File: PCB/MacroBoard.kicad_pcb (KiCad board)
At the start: 2 copper layers, 192.1 x 82.6 mm, 57 parts, among them J1 Pwr, J2 UART, J3 ADC, J4 I2C, J5 B In, J6 Switch, SW0 SW_Push, SW1 SW_Push, SW10 SW_Push, SW11 SW_Push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

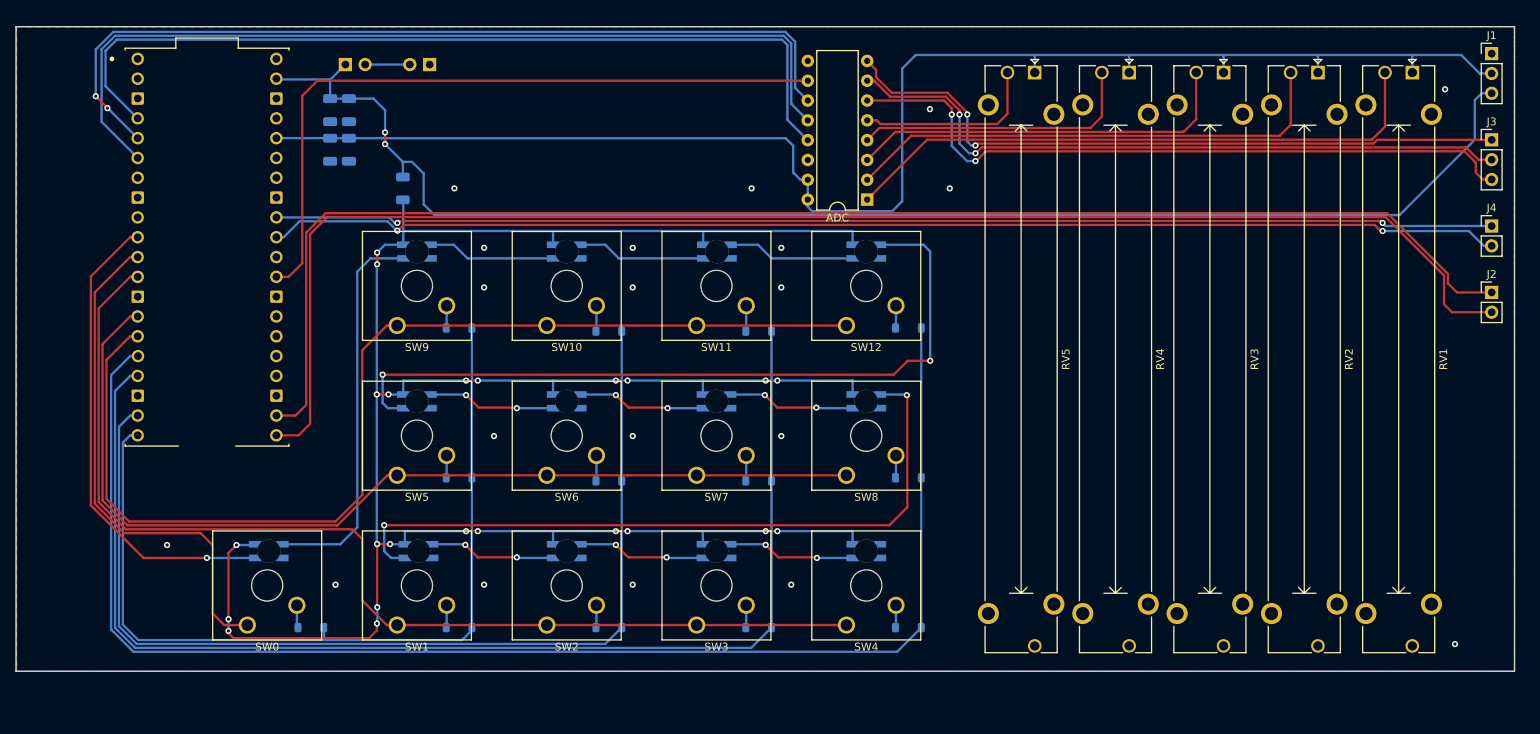
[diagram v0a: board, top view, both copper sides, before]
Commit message: Increased power tracks width
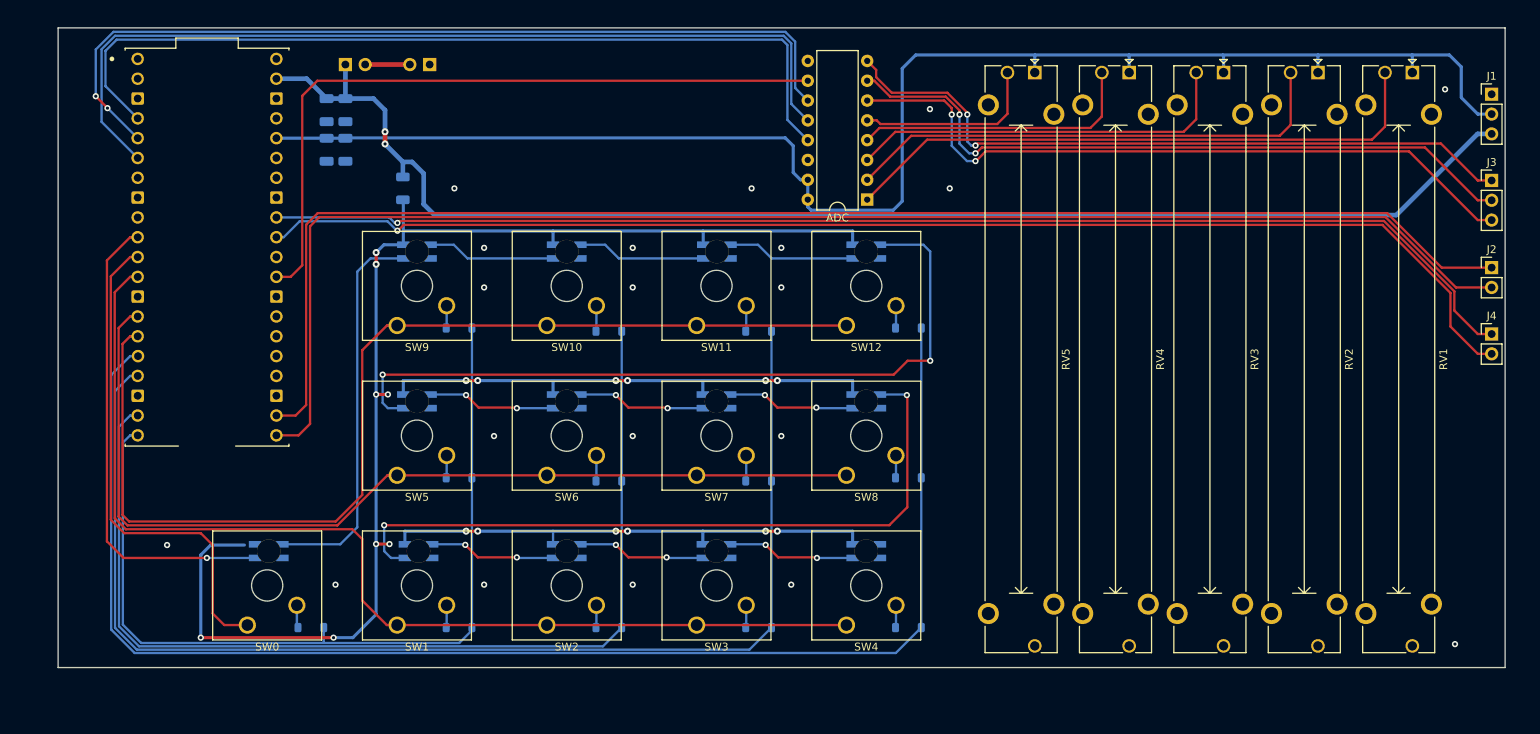
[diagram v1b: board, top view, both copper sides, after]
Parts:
- moved J4 13.8 mm to (209.2, 56.8)
- moved J3 5.21 mm to (209.2, 37.1)
- moved J1 5.21 mm to (209.2, 26.0)
- moved J2 3.18 mm to (209.2, 48.3)
- moved C1 0.45 mm to (62.2, 33.1)
- moved C2 0.45 mm to (59.8, 33.1)
- moved C3 0.45 mm to (59.8, 28.1)
- moved C4 0.45 mm to (62.2, 28.1)
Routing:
- net I2C_SDA_E: track 158.6 -> 166.8 mm, vias 2 -> 1
- net I2C_SCL_E: track 156.5 -> 163.6 mm, vias 2 -> 1
- net 5V: track 183.5 -> 178.6 mm
- net 3V3: track 194.6 -> 197.9 mm
- net UART_TX: track 188.8 -> 186.0 mm
- net CH_6: track 87.4 -> 89.5 mm
- net CH_7: track 87.6 -> 89.3 mm
- net ROW_2: track 125.4 -> 123.7 mm
- net ROW_1: track 140.4 -> 138.7 mm
- net ROW_3: track 138.5 -> 136.8 mm
- net ROW_4: track 65.8 -> 64.1 mm
- net UART_RX: track 184.4 -> 183.0 mm
- net CH_5: track 88.8 -> 90.3 mm
- net LED: track 290.8 -> 291.8 mm, vias 23 -> 20
- net COL_1: track 112.4 -> 113.1 mm
- removed copper zone on B.Cu, net GND
- removed copper zone on F.Cu, net GND
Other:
- board size 192.1 x 82.6 mm -> 185.5 x 82 mm

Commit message: New LED Footprint, new routings
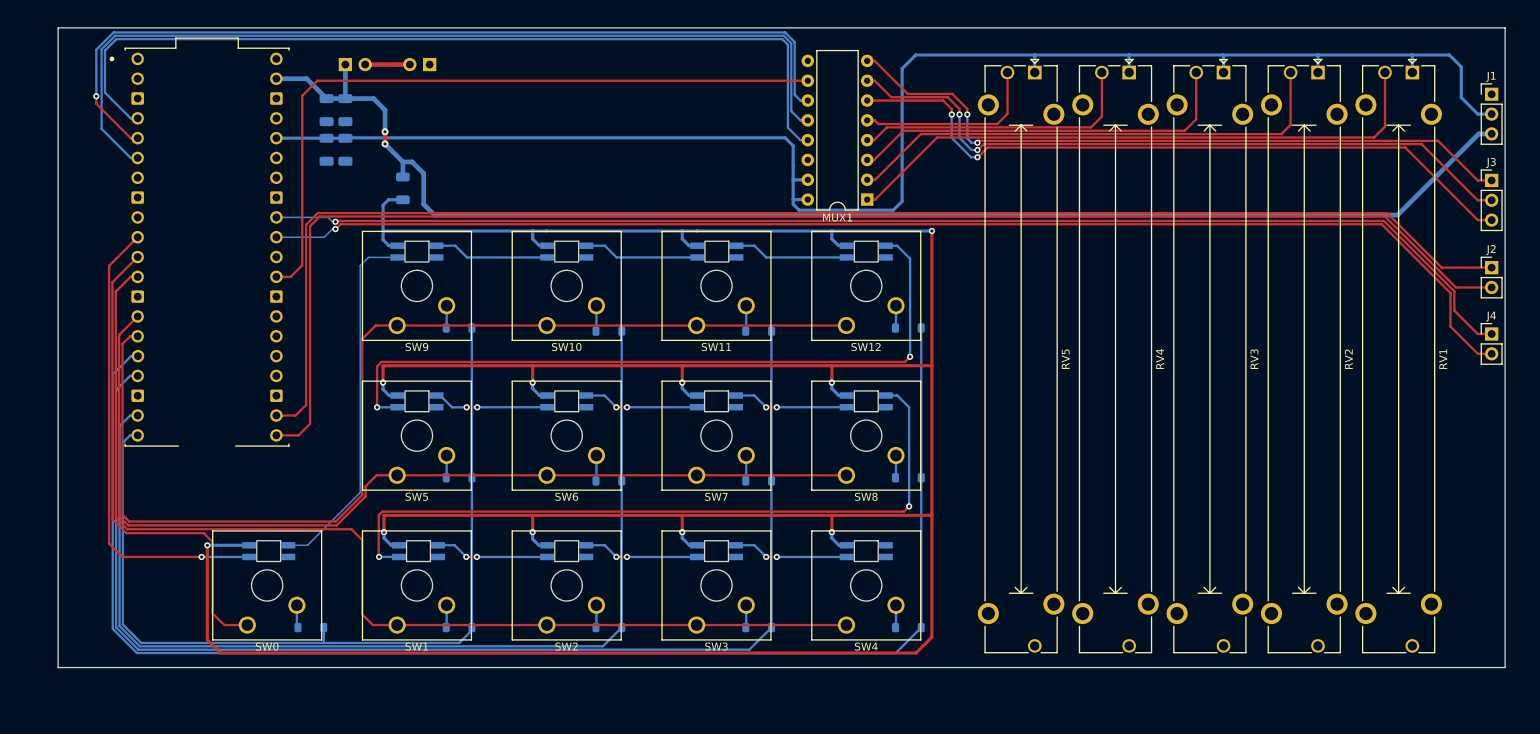
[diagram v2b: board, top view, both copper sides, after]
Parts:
- L0, L1, L10, L11, L12, L2, L3, L4, L5, L6, L7, L8, L9: value SK6812MINI -> SK6812MINI-E; footprint Custom:LED_SK6812MINI_PLCC4_3.5x3.5mm_P1.75mm -> LibraryTool:SK6812MINIE
- renumbered ADC to MUX1
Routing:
- net LED: track 291.8 -> 436.2 mm, vias 20 -> 10
- net LED_3: track 98.3 -> 93.1 mm
- net 3V3: track 197.9 -> 202.0 mm
- net LED_2: track 49.9 -> 46.3 mm
- net Net-(L3-DOUT): track 16.4 -> 14.8 mm
- net Net-(L2-DOUT): track 16.4 -> 14.8 mm
- net Net-(L11-DOUT): track 16.4 -> 14.8 mm
- net Net-(L10-DOUT): track 16.5 -> 14.9 mm
- net Net-(L10-DIN): track 16.4 -> 14.8 mm
- net LED_1: track 61.1 -> 59.5 mm
- net Net-(L1-DOUT): track 16.2 -> 14.6 mm
- net Net-(L7-DOUT): track 16.4 -> 14.8 mm
- net Net-(L6-DOUT): track 16.4 -> 14.8 mm
- net Net-(L5-DOUT): track 16.4 -> 14.8 mm
- net CLK: track 111.9 -> 113.2 mm
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
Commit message: Fixed some routing issues, changed some tracks to reduce interference, added silkscreen
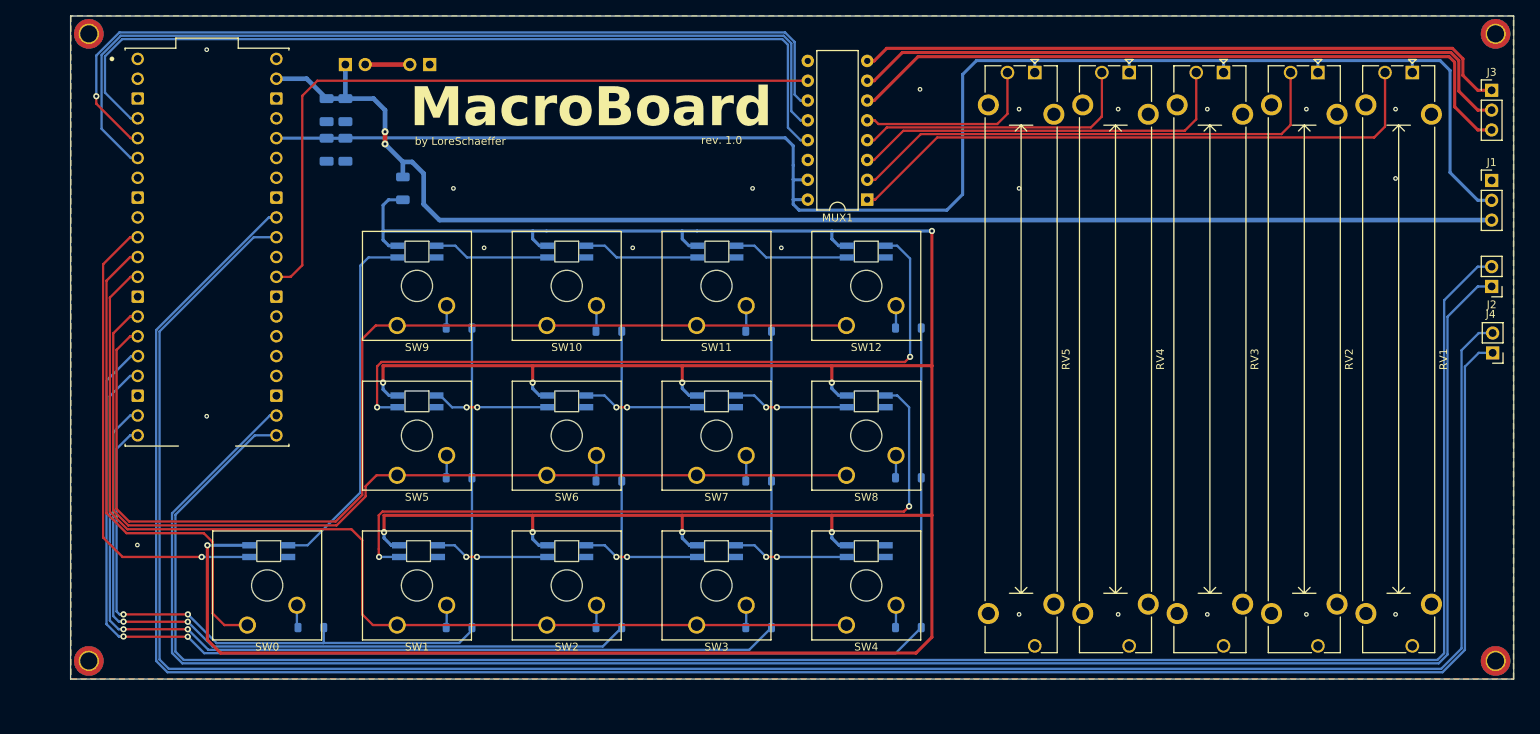
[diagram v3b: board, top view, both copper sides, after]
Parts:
- added REF**: MountingHole_2.2mm_M2_DIN965_Pad_TopBottom, MountingHole:MountingHole_2.2mm_M2_DIN965_Pad_TopBottom, F.Cu at (209.7, 18.3)
- added REF**: MountingHole_2.2mm_M2_DIN965_Pad_TopBottom, MountingHole:MountingHole_2.2mm_M2_DIN965_Pad_TopBottom, F.Cu at (29.3, 18.3)
- added REF**: MountingHole_2.2mm_M2_DIN965_Pad_TopBottom, MountingHole:MountingHole_2.2mm_M2_DIN965_Pad_TopBottom, F.Cu at (209.7, 98.7)
- added REF**: MountingHole_2.2mm_M2_DIN965_Pad_TopBottom, MountingHole:MountingHole_2.2mm_M2_DIN965_Pad_TopBottom, F.Cu at (29.3, 98.7)
- moved J3 11.6 mm to (209.2, 25.5)
- moved J1 11.0 mm to (209.2, 37.1)
- moved J4 2.42 mm to (209.3, 59.2), turned to 180 degrees
- moved J2 2.41 mm to (209.2, 50.7), turned to 180 degrees
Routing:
- net I2C_SCL_E: track 163.5 -> 273.9 mm, vias 1 -> 0
- net I2C_SDA_E: track 165.9 -> 273.7 mm, vias 1 -> 0
- net UART_RX: track 183.0 -> 251.6 mm
- net UART_TX: track 186.0 -> 251.3 mm
- net 3V3: track 202.0 -> 206.9 mm
- net CH_7: track 88.8 -> 84.2 mm, vias 2 -> 0
- net 5V: track 178.6 -> 174.6 mm
- net CH_6: track 89.2 -> 86.9 mm, vias 2 -> 0
- net ROW_4: track 63.4 -> 64.6 mm
- net LED_1: track 59.5 -> 60.7 mm
- net ROW_2: track 123.7 -> 124.9 mm
- net COL_4: track 181.5 -> 182.3 mm, vias 0 -> 2
- net COL_3: track 158.3 -> 159.0 mm, vias 0 -> 2
- net ROW_3: track 137.5 -> 138.1 mm
- net ROW_1: track 139.5 -> 140.2 mm
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- added copper zone on B.Cu, net GND
- added copper zone on F.Cu, net GND
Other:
- board size 185.5 x 82 mm -> 185 x 85 mm
- board text added: "MacroBoard"
- board text added: "by LoreSchaeffer"
- board text added: "rev. 1.0"

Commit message: Updated PCB, increased tracks and vias size, added level converter
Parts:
- added C5: 10uF, Capacitor_SMD:C_1206_3216Metric, B.Cu at (116.3, 36.3)
- added C6: 100uF, Capacitor_SMD:C_1206_3216Metric, B.Cu at (116.3, 38.6)
- added Q1: 2N7002, Package_TO_SOT_SMD:SOT-23, B.Cu at (74.9, 37.6)
- added R2: 10k, Resistor_SMD:R_1206_3216Metric, B.Cu at (74.3, 33.4)
- added R3: 10k, Resistor_SMD:R_1206_3216Metric, B.Cu at (81.0, 40.1)
- added REF**: MountingHole_2.2mm_M2_DIN965_Pad_TopBottom, MountingHole:MountingHole_2.2mm_M2_DIN965_Pad_TopBottom, F.Cu at (99.1, 36.8)
- RPPW1: footprint Raspberry Pi Pico:MODULE_SC0918 -> RPiP:MODULE_SC0918
- moved REF** 4.83 mm to (29.5, 103.5)
- moved REF** 4.83 mm to (209.6, 103.5)
- moved R1 4.57 mm to (65.0, 38.2)
- moved C1 2.41 mm to (59.8, 33.1)
- moved C2 2.41 mm to (57.4, 33.1)
- moved J1 1.52 mm to (209.2, 35.6)
- moved C3 1.07 mm to (59.8, 27.0)
- moved C4 1.07 mm to (62.2, 27.0)
- moved REF** 0.18 mm to (29.5, 18.4)
- moved REF** 0.18 mm to (209.6, 18.4)
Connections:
- RPPW1 pad 10: LED_1 -> LVL_CON
- RV1 pad MP: unconnected-(RV1-MountPin-PadMP) -> GND
- RV2 pad MP: unconnected-(RV2-MountPin-PadMP) -> GND
- RV3 pad MP: unconnected-(RV3-MountPin-PadMP) -> GND
- RV4 pad MP: unconnected-(RV4-MountPin-PadMP) -> GND
- RV5 pad MP: unconnected-(RV5-MountPin-PadMP) -> GND
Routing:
- net LVL_CON: track 0.00 -> 100.1 mm, vias 0 -> 3
- net LED_1: track 60.7 -> 78.7 mm, vias 1 -> 4
- net 3V3: track 206.9 -> 218.8 mm
- net LED: track 436.2 -> 425.0 mm
- net ROW_1: track 140.2 -> 129.4 mm
- net I2C_SCL_E: track 273.9 -> 283.3 mm
- net ROW_2: track 124.9 -> 117.0 mm
- net I2C_SDA_E: track 273.7 -> 281.5 mm
- net UART_RX: track 251.6 -> 257.3 mm
- net COL_4: track 182.3 -> 187.9 mm
- net CLK: track 112.8 -> 107.9 mm
- net UART_TX: track 251.3 -> 255.4 mm
- net D_OUT: track 116.8 -> 113.0 mm
- net COL_3: track 159.0 -> 161.7 mm
- net COL_2: track 133.4 -> 135.9 mm
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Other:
- board size 185 x 85 mm -> 185 x 90 mm
- board text added: "JLCJLCJLCJLC"

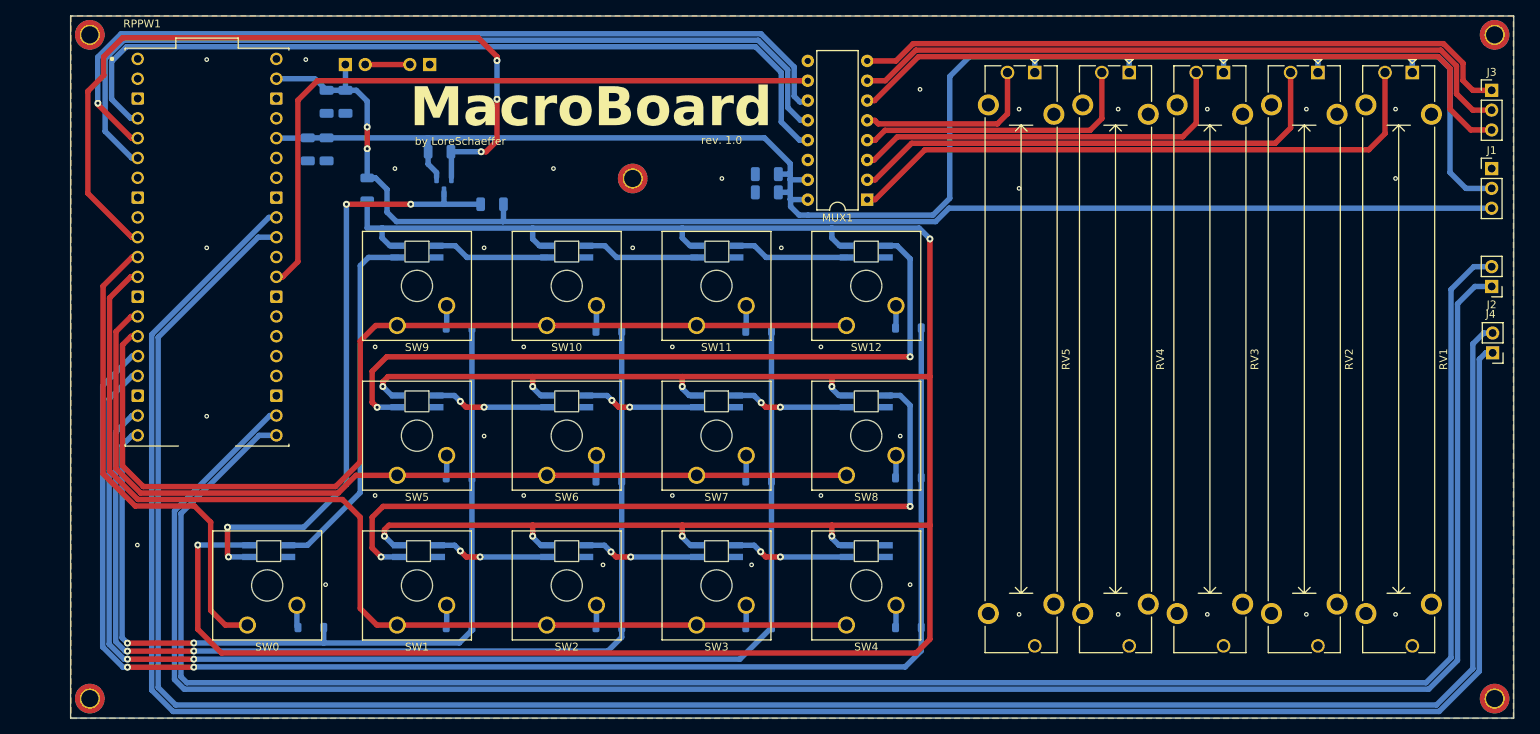
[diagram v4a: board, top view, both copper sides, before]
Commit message: Added silkscreen
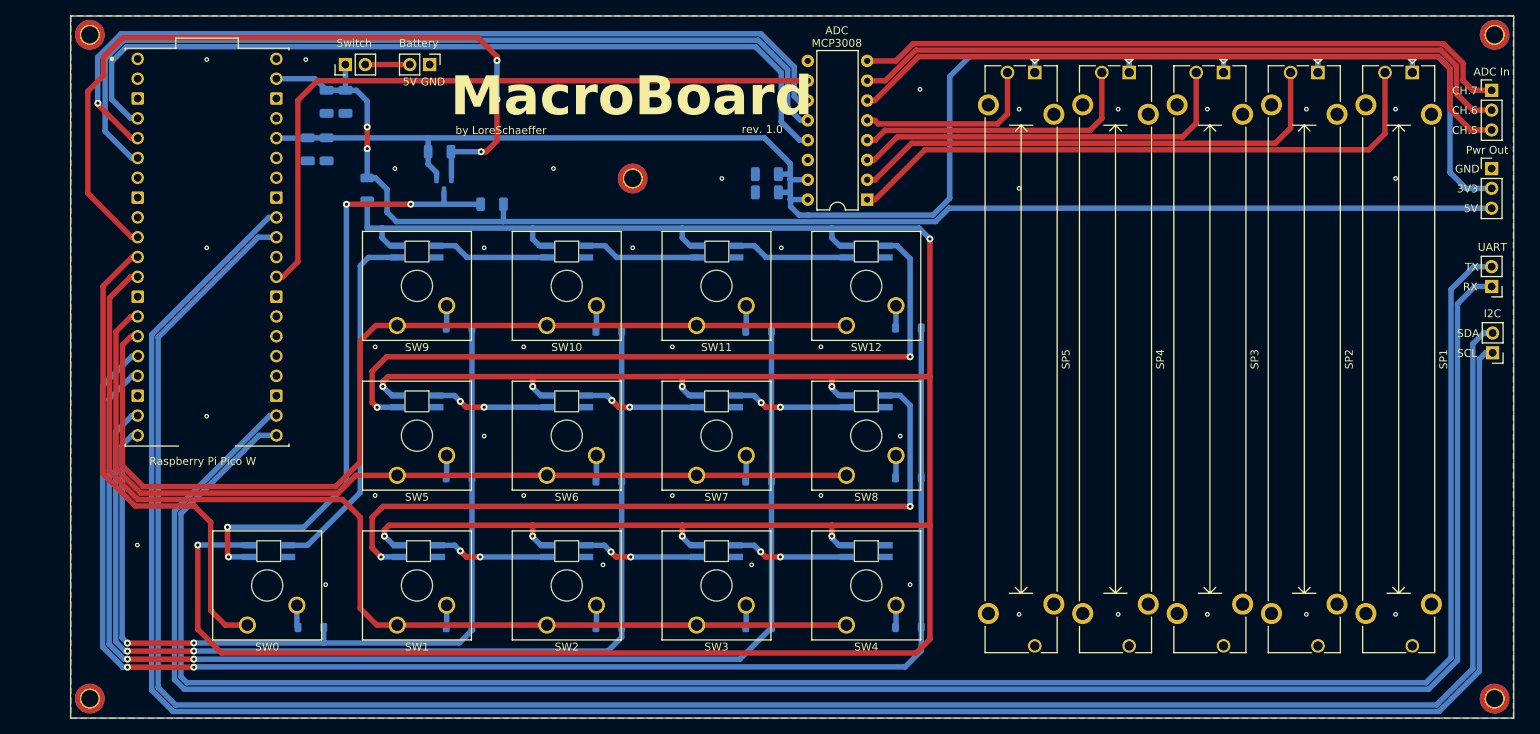
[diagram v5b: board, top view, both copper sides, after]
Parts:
- J5, J6: moved to F.Cu
- turned J5 to -90 degrees
- turned J6 to 90 degrees
- renumbered RV1 to SP1, RV2 to SP2, RV3 to SP3, RV4 to SP4, RV5 to SP5
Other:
- board text added: "2N002"
- board text added: "3V3"
- board text added: "5V"
- board text added: "ADC In"
- board text added: "ADC MCP3008"
- board text added: "Battery"
- board text added: "CH.5"
- board text added: "CH.6"
- board text added: "CH.7"
- board text added: "GND"
- board text added: "I2C"
- board text added: "Pwr Out"
- board text added: "RX"
- board text added: "Raspberry Pi Pico W"
- board text added: "SCL"
- board text added: "SDA"
- board text added: "Switch"
- board text added: "TX"
- board text added: "UART"
